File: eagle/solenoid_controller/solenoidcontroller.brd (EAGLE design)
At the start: 100 x 80 mm, 44 parts, among them J1 ARDUINO_R3_SHIELD, Q1 PMV45EN, Q2 PMV45EN, Q3 PMV45EN, Q4 PMV45EN, Q5 PMV45EN, Q6 PMV45EN

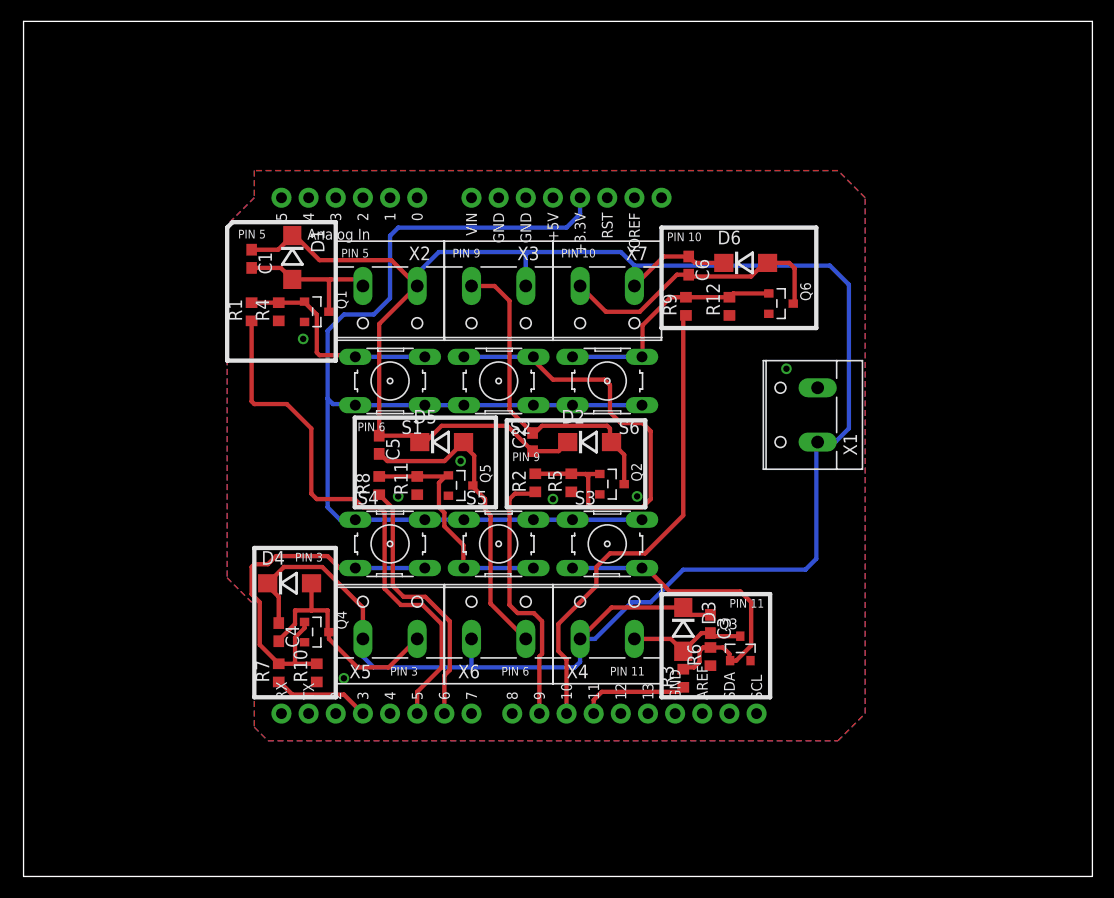
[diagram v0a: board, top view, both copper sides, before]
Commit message: Cleaned up Baker's already A-OK board. Switched kickback components to bottom to minimimze copper length, fattened up power traces and reduced length, added text on top layer, re-numbered the solenoid terminals, stiched ground.
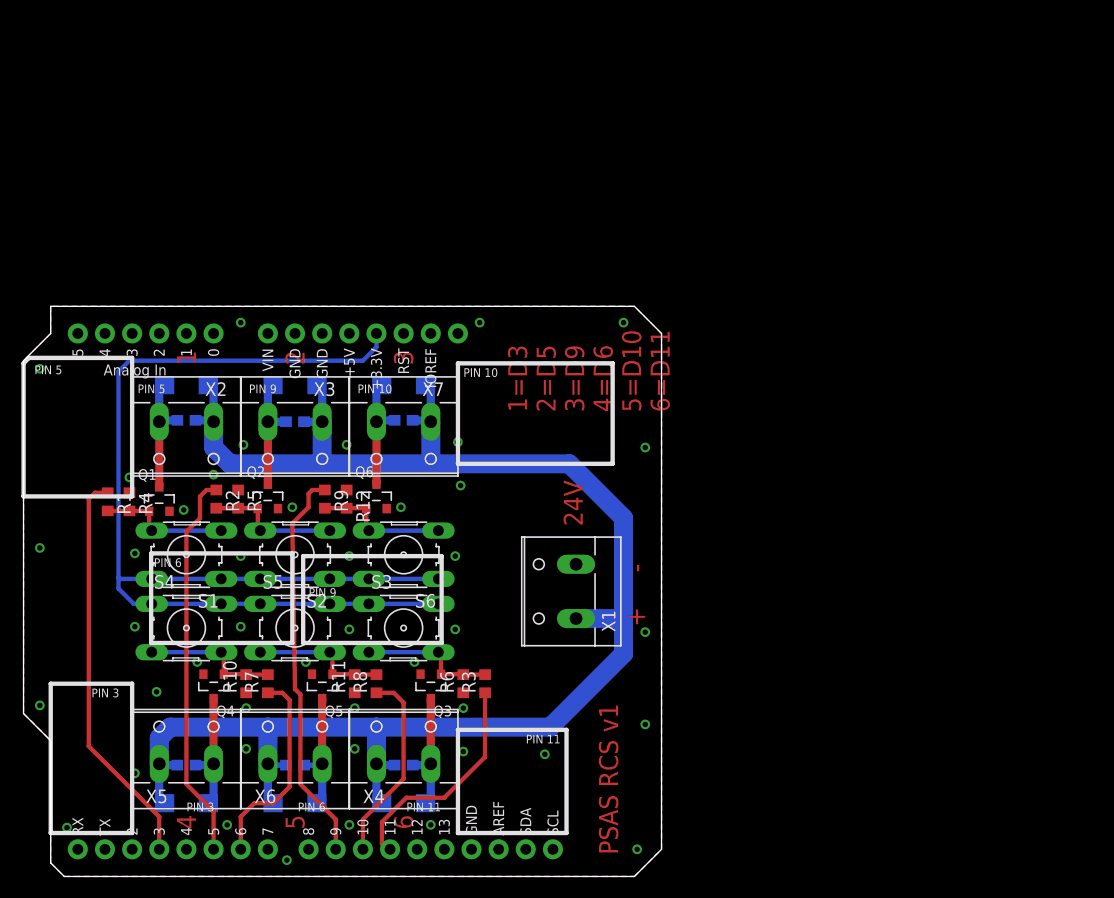
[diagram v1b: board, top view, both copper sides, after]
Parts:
- moved Q6 41.9 mm to (33.0, 35.6), turned to 0 degrees
- moved R12 40.1 mm to (30.2, 35.3), turned to 270 degrees
- moved R9 38.3 mm to (28.2, 35.3), turned to 270 degrees
- moved D5 36.5 mm to (25.4, 6.86), flipped to the bottom, turned to 180 degrees
- moved D6 34.0 mm to (35.6, 46.0), flipped to the bottom
- moved Q2 32.2 mm to (22.9, 35.6), turned to 0 degrees
- moved C3 31.6 mm to (35.6, 10.4), flipped to the bottom, turned to 180 degrees
- moved R5 31.2 mm to (20.1, 35.3), turned to 270 degrees
- moved C5 31.0 mm to (25.4, 10.4), flipped to the bottom, turned to 180 degrees
- moved D3 30.8 mm to (35.6, 6.86), flipped to the bottom, turned to 180 degrees
- moved C6 30.3 mm to (35.6, 42.7), flipped to the bottom, turned to 0 degrees
- moved R2 29.9 mm to (18.0, 35.3), turned to 270 degrees
- moved Q3 29.2 mm to (38.1, 17.8), turned to 180 degrees
- moved D2 28.1 mm to (25.4, 46.0), flipped to the bottom
- moved X1 28.0 mm to (51.1, 26.7)
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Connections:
- net N$15 renamed 6
- removed net N$13: J1.D9, R2.1
- removed net N$14: J1.D5, R1.1
- removed net N$16: J1.D10, R9.1
- removed net N$17: J1.D3, R7.1
- removed net N$18: J1.D6, R8.1
- new net 1: J1.D3, R1.1
- new net 2: J1.D5, R2.1
- new net 3: J1.D9, R9.1
- new net 4: J1.D6, R7.1
- new net 5: J1.D10, R8.1
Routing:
- net +24V: track 224.6 -> 158.2 mm
- net N$14: track 51.0 -> 0.00 mm
- net N$16: track 44.4 -> 0.00 mm
- net 1: track 0.00 -> 37.5 mm
- net 3: track 0.00 -> 37.2 mm
- net 2: track 0.00 -> 36.4 mm
- net N$1: track 43.6 -> 12.7 mm
- net N$13: track 25.0 -> 0.00 mm
- net N$18: track 24.8 -> 0.00 mm
- net N$7: track 35.0 -> 12.9 mm
- net N$3: track 30.8 -> 11.2 mm
- net 4: track 0.00 -> 19.2 mm
- net N$2: track 31.4 -> 12.8 mm
- net 5: track 0.00 -> 18.2 mm
- net N$10: track 29.8 -> 11.9 mm
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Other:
- board size 100 x 80 mm -> 59.7 x 53.3 mm
- board text added: "+"
- board text added: "-"
- board text added: "1"
- board text added: "1=D3 2=D5 3=D9 4=D6 5=D10 6=D11"
- board text added: "2"
- board text added: "24V"
- board text added: "3"
- board text added: "4"
- board text added: "5"
- board text added: "6"
- board text added: "PSAS RCS v1"

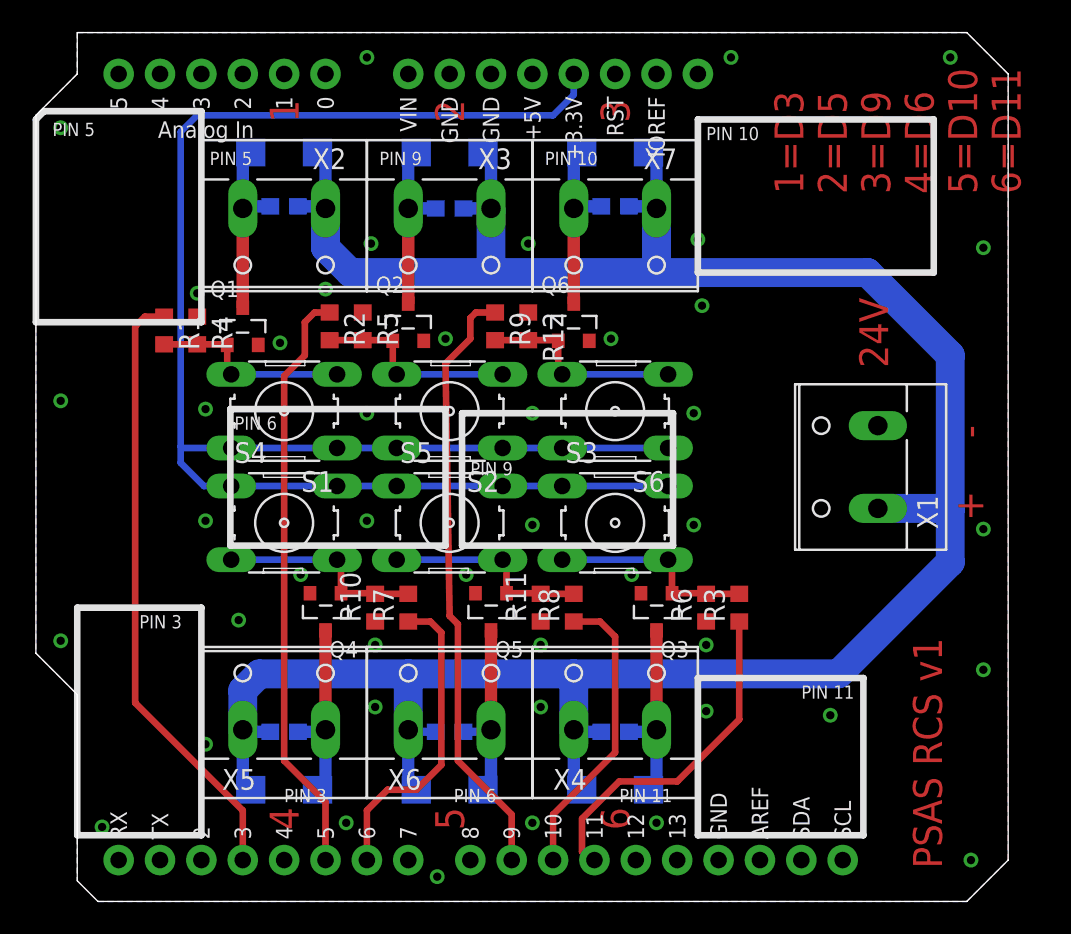
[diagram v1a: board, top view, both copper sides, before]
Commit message: Updated solenoid controller board; moved all SMD components to bottom layer and power traces to top layer.
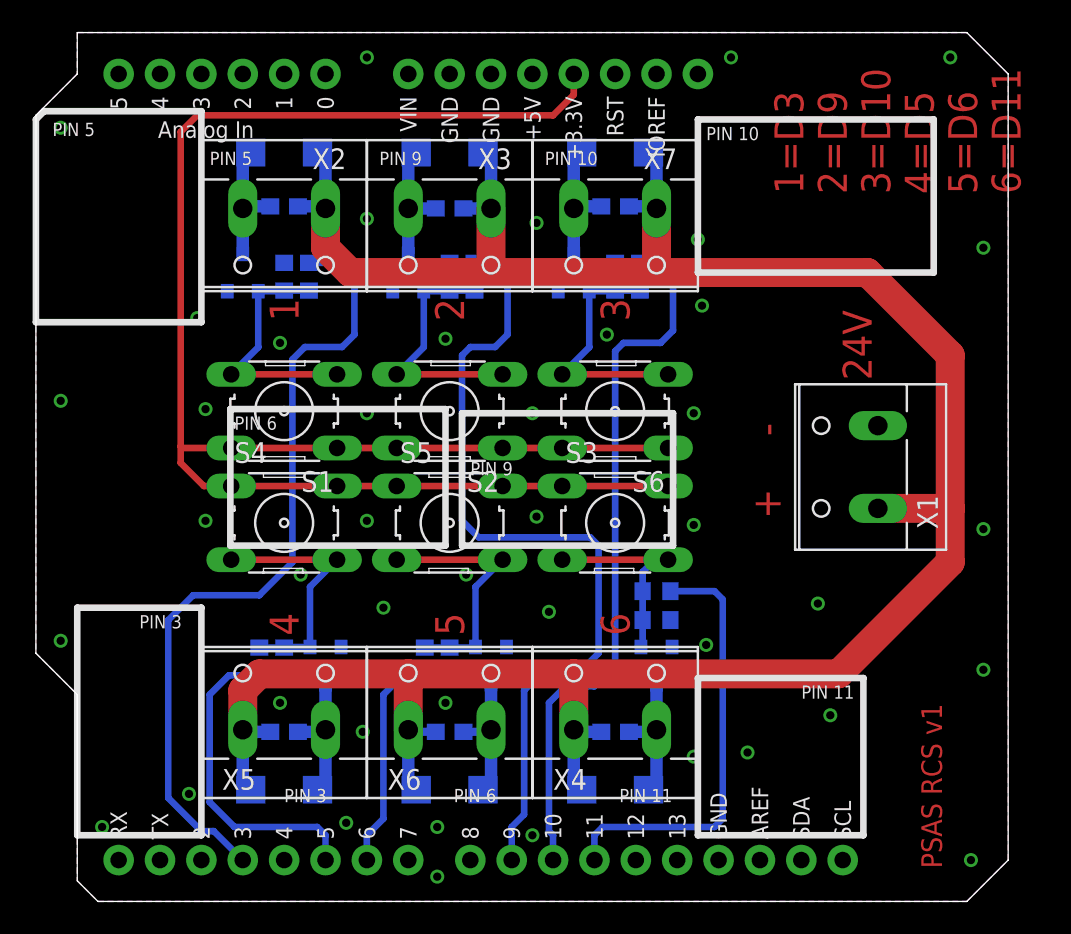
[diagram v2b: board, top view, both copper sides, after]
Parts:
- moved R8 9.72 mm to (23.9, 14.7), flipped to the bottom
- moved R7 9.72 mm to (13.7, 14.7), flipped to the bottom
- moved R1 9.48 mm to (16.8, 38.4), flipped to the bottom
- moved R9 9.40 mm to (37.1, 38.4), flipped to the bottom
- moved R2 9.40 mm to (26.9, 38.4), flipped to the bottom
- moved R11 6.49 mm to (25.4, 14.7), flipped to the bottom
- moved R10 6.49 mm to (15.2, 14.7), flipped to the bottom
- moved R4 6.27 mm to (15.2, 38.4), flipped to the bottom
- moved R12 6.14 mm to (35.6, 38.4), flipped to the bottom
- moved R5 6.14 mm to (25.4, 38.4), flipped to the bottom
- moved R3 5.18 mm to (38.1, 19.1), flipped to the bottom, turned to 0 degrees
- moved Q3 3.30 mm to (38.1, 14.5), flipped to the bottom
- moved Q4 3.30 mm to (17.8, 14.5), flipped to the bottom
- moved Q5 3.30 mm to (27.9, 14.5), flipped to the bottom
- moved Q1 3.30 mm to (12.7, 38.6), flipped to the bottom
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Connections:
- net 2: now also J1.D9; no longer J1.D5
- net 3: now also J1.D10; no longer J1.D9
- net 4: now also J1.D5; no longer J1.D6
- net 5: now also J1.D6; no longer J1.D10
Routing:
- net 2: track 36.4 -> 51.3 mm
- net 1: track 37.5 -> 49.6 mm
- net 3: track 37.2 -> 43.8 mm
- net 6: track 21.1 -> 26.7 mm
- net 5: track 18.2 -> 13.6 mm
- net N$8: track 11.7 -> 8.37 mm
- net N$6: track 11.4 -> 8.12 mm
- net N$4: track 11.7 -> 8.37 mm
- net N$10: track 11.9 -> 8.62 mm
- net N$5: track 12.3 -> 15.4 mm
- net N$3: track 11.2 -> 8.12 mm
- net N$12: track 11.2 -> 8.17 mm
- net N$11: track 12.6 -> 15.4 mm
- net N$7: track 12.9 -> 15.7 mm
- net N$1: track 12.7 -> 15.4 mm
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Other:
- board text added: "1=D3 2=D9 3=D10 4=D5 5=D6 6=D11"
- board text removed: "1=D3 2=D5 3=D9 4=D6 5=D10 6=D11"
